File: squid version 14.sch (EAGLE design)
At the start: 61 parts, among them J2 ATMEL_PROGRAMMER_HEADERNL, U2 MCP73832

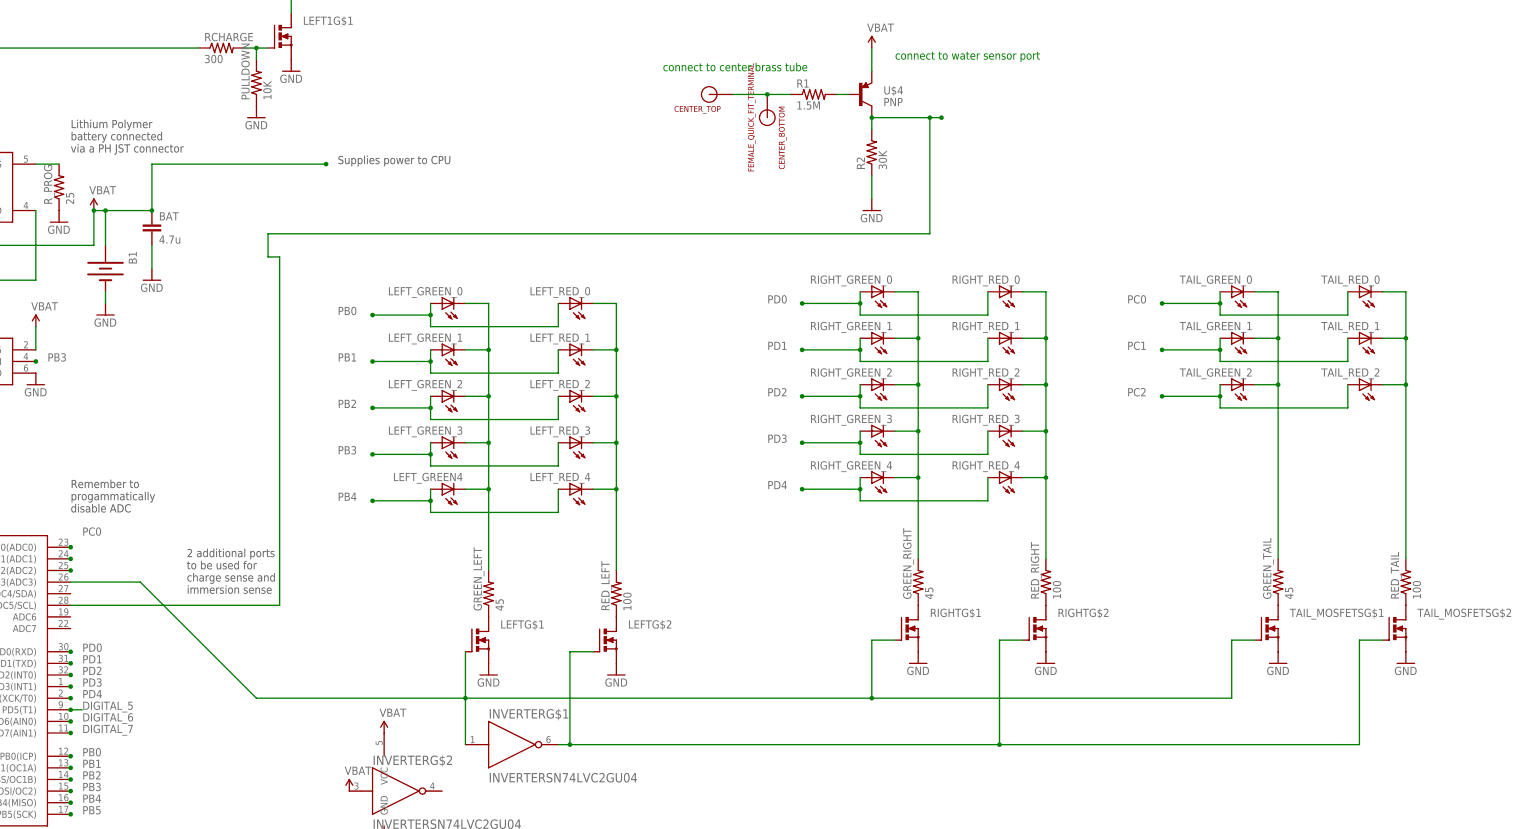
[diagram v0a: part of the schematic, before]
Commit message: put RG TH lights in rear
Rearranged board to hold TH parts in rear.
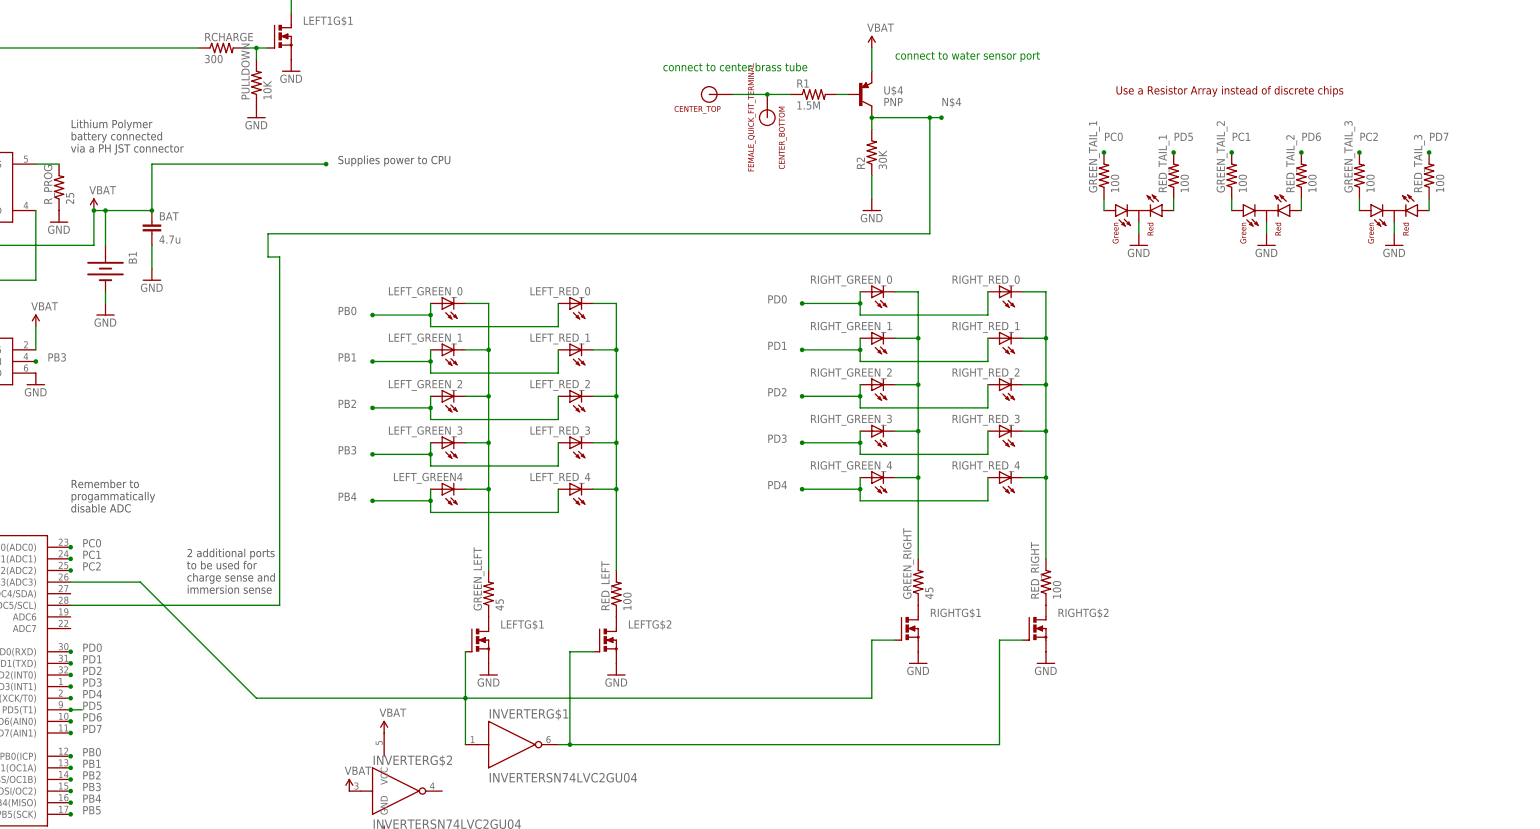
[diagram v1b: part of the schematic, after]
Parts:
- removed GREEN_TAIL: 45, SparkFun-Passives:RESISTOR0805-RES
- removed RED_TAIL: 100, SparkFun-Passives:RESISTOR0805-RES
- removed TAIL_GREEN_0, TAIL_GREEN_1, TAIL_GREEN_2, TAIL_RED_0, TAIL_RED_1, TAIL_RED_2: (no value), ERIC:LEDPLCC2
- removed TAIL_MOSFETS: MOSFET_N_DUAL, ERIC:MOSFET_N_DUAL
- added CENTER, U$13, U$7: LED_RED_GREEN_CC, ERIC:LED_RED_GREEN_CC
- added GREEN_TAIL_1, GREEN_TAIL_2, GREEN_TAIL_3, RED_TAIL_1, RED_TAIL_2, RED_TAIL_3: 100, SparkFun-Passives:RESISTOR0805-RES
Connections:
- removed net DIGITAL_5: U1.PD5(T1)
- removed net DIGITAL_6: U1.PD6(AIN0)
- removed net DIGITAL_7: U1.PD7(AIN1)
- removed net N$13: GREEN_TAIL.1, TAIL_MOSFETSG$1.D
- removed net N$18: RED_TAIL.1, TAIL_MOSFETSG$2.D
- removed net N$19: GREEN_TAIL.2, TAIL_GREEN_0.C, TAIL_GREEN_1.C, TAIL_GREEN_2.C
- new net N$17: GREEN_TAIL_1.1, U$7.GREEN
- new net N$22: GREEN_TAIL_3.1, U$13.GREEN
- new net N$23: RED_TAIL_1.1, U$7.RED
- new net N$24: CENTER.RED, RED_TAIL_2.1
- new net N$25: RED_TAIL_3.1, U$13.RED
- new net PD5: RED_TAIL_1.2, U1.PD5(T1)
- new net PD6: RED_TAIL_2.2, U1.PD6(AIN0)
- new net PD7: RED_TAIL_3.2, U1.PD7(AIN1)
- net GND: now also CENTER.C, U$13.C, U$7.C; no longer TAIL_MOSFETSG$1.S, TAIL_MOSFETSG$2.S
- net N$2: no longer TAIL_MOSFETSG$2.G
- net N$20: now also CENTER.GREEN, GREEN_TAIL_2.1; no longer RED_TAIL.2, TAIL_RED_0.C, TAIL_RED_1.C, TAIL_RED_2.C
- net N$7: no longer TAIL_MOSFETSG$1.G
- net PC0: now also GREEN_TAIL_1.2; no longer TAIL_GREEN_0.A, TAIL_RED_0.A
- net PC1: now also GREEN_TAIL_2.2; no longer TAIL_GREEN_1.A, TAIL_RED_1.A
- net PC2: now also GREEN_TAIL_3.2; no longer TAIL_GREEN_2.A, TAIL_RED_2.A
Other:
- note added: "Use a Resistor Array instead of discrete chips"

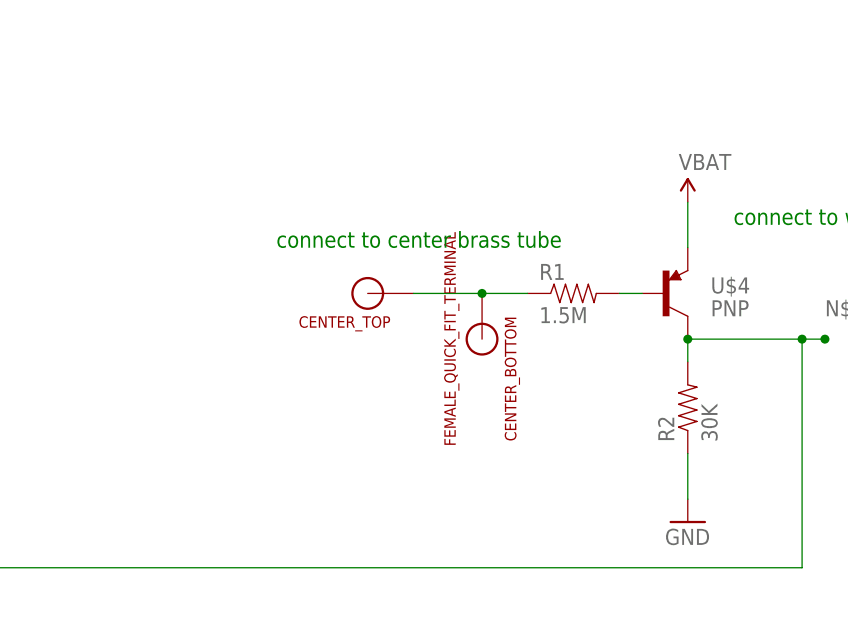
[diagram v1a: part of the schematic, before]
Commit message: disconnect top center tube holder
Does not need an electrical connection
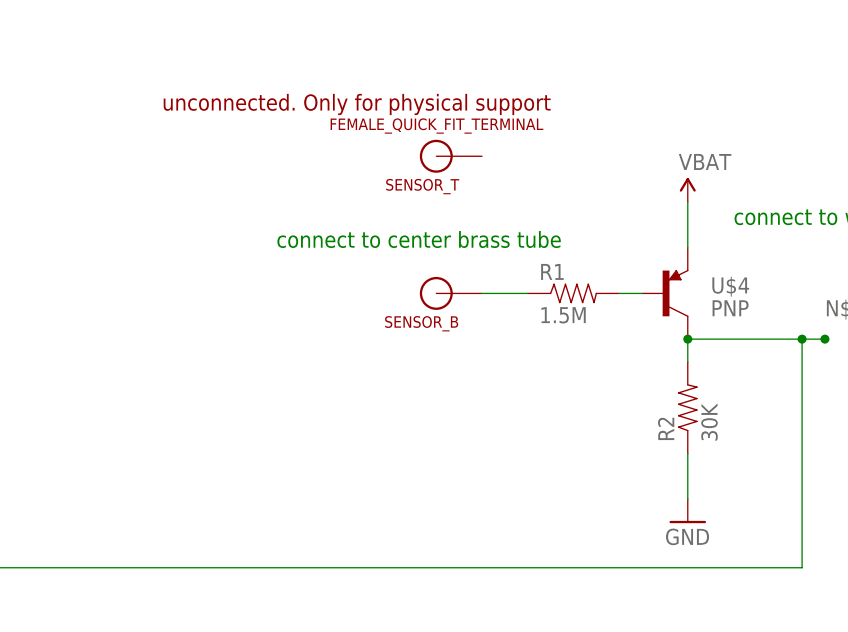
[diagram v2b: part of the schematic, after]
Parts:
- removed CENTER_BOTTOM, CENTER_TOP: FEMALE_QUICK_FIT_TERMINAL, Keystone:FEMALE_QUICK_FIT_TERMINAL
- added SENSOR_B, SENSOR_T: FEMALE_QUICK_FIT_TERMINAL, Keystone:FEMALE_QUICK_FIT_TERMINAL
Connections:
- net N$9: now also SENSOR_B.P$1; no longer CENTER_BOTTOM.P$1, CENTER_TOP.P$1
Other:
- note added: "unconnected. Only for physical support"
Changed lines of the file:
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@@
 <part name="RIGHT_RED_4" library="ERIC" deviceset="LED" device="PLCC2"/>
 <part name="RIGHT_RED_0" library="ERIC" deviceset="LED" device="PLCC2"/>
-<part name="CENTER_BOTTOM" library="Keystone" deviceset="FEMALE_QUICK_FIT_TERMINAL" device=""/>
-<part name="CENTER_TOP" library="Keystone" deviceset="FEMALE_QUICK_FIT_TERMINAL" device="" value=""/>
+<part name="SENSOR_T" library="Keystone" deviceset="FEMALE_QUICK_FIT_TERMINAL" device=""/>
+<part name="SENSOR_B" library="Keystone" deviceset="FEMALE_QUICK_FIT_TERMINAL" device="" value=""/>
 <part name="GND11" library="SparkFun" deviceset="GND" device=""/>
 <part name="U$14" library="ERIC" deviceset="VBAT" device=""/>
@@
 <text x="109.22" y="190.5" size="1.778" layer="91">RESET LOW when charging</text>
 <text x="330.2" y="167.64" size="1.778" layer="94">Use a Resistor Array instead of discrete chips</text>
+<text x="218.44" y="187.96" size="1.778" layer="94">unconnected. Only for physical support</text>
 </plain>
 <instances>
@@
 <instance part="RIGHT_RED_4" gate="G$1" x="307.34" y="83.82" rot="R90"/>
 <instance part="RIGHT_RED_0" gate="G$1" x="307.34" y="124.46" rot="R90"/>
-<instance part="CENTER_BOTTOM" gate="G$1" x="254" y="162.56" rot="R270"/>
-<instance part="CENTER_TOP" gate="G$1" x="241.3" y="167.64" rot="R180"/>
+<instance part="SENSOR_T" gate="G$1" x="248.92" y="182.88" rot="R180"/>
+<instance part="SENSOR_B" gate="G$1" x="248.92" y="167.64" rot="R180"/>
 <instance part="INVERTER" gate="G$2" x="172.72" y="15.24"/>
 <instance part="INVERTER" gate="G$3" x="170.18" y="20.32"/>
@@
 </segment>
 </net>
-<net name="N$9" class="0">
-<segment>
-<pinref part="R1" gate="G$1" pin="1"/>
-<pinref part="CENTER_BOTTOM" gate="G$1" pin="P$1"/>
-<wire x1="259.08" y1="167.64" x2="254" y2="167.64" width="0.1524" layer="91"/>
-<pinref part="CENTER_TOP" gate="G$1" pin="P$1"/>
-<wire x1="246.38" y1="167.64" x2="254" y2="167.64" width="0.1524" layer="91"/>
-<junction x="254" y="167.64"/>
-</segment>
-</net>
 <net name="N$21" class="0">
 <segment>
@@
 </segment>
 </net>
+<net name="N$9" class="0">
+<segment>
+<pinref part="R1" gate="G$1" pin="1"/>
+<pinref part="SENSOR_B" gate="G$1" pin="P$1"/>
+<wire x1="254" y1="167.64" x2="259.08" y2="167.64" width="0.1524" layer="91"/>
+</segment>
+</net>

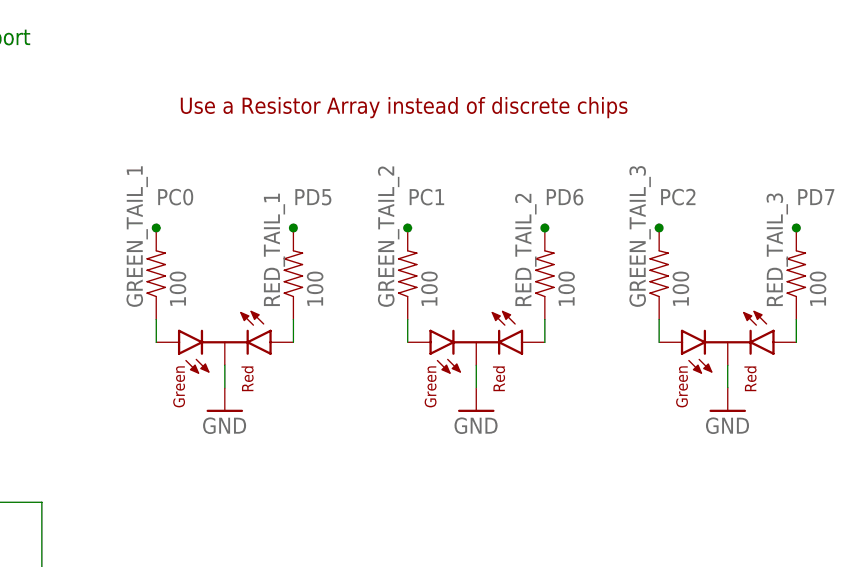
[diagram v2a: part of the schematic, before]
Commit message: assign values of ballast resistors
Put proper values of ballast resistors into schematic
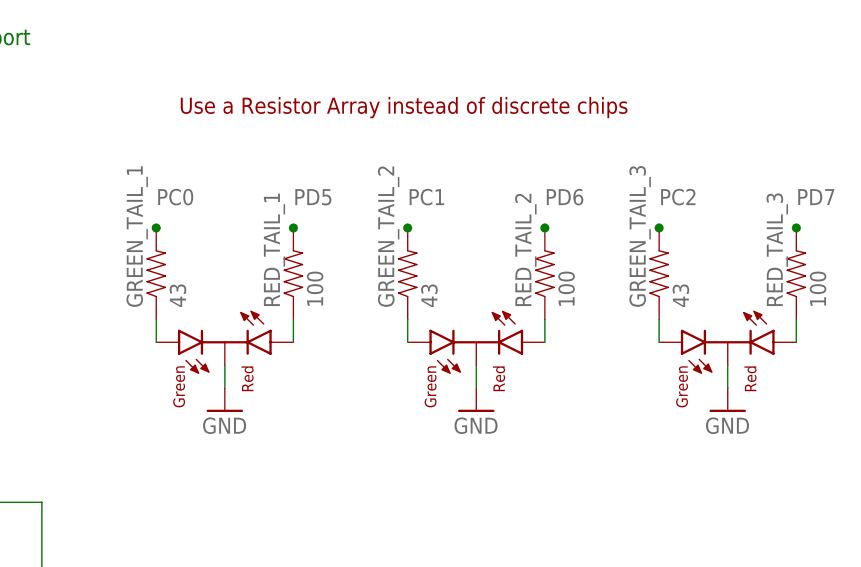
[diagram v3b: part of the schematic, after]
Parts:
- GREEN_TAIL_1, GREEN_TAIL_2, GREEN_TAIL_3: value 100 -> 43
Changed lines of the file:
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@@
 <part name="GND18" library="SparkFun" deviceset="GND" device=""/>
 <part name="GND22" library="SparkFun" deviceset="GND" device=""/>
-<part name="GREEN_TAIL_1" library="SparkFun-Passives" deviceset="RESISTOR" device="0805-RES" value="100"/>
-<part name="GREEN_TAIL_2" library="SparkFun-Passives" deviceset="RESISTOR" device="0805-RES" value="100"/>
-<part name="GREEN_TAIL_3" library="SparkFun-Passives" deviceset="RESISTOR" device="0805-RES" value="100"/>
+<part name="GREEN_TAIL_1" library="SparkFun-Passives" deviceset="RESISTOR" device="0805-RES" value="43"/>
+<part name="GREEN_TAIL_2" library="SparkFun-Passives" deviceset="RESISTOR" device="0805-RES" value="43"/>
+<part name="GREEN_TAIL_3" library="SparkFun-Passives" deviceset="RESISTOR" device="0805-RES" value="43"/>
 <part name="RED_TAIL_1" library="SparkFun-Passives" deviceset="RESISTOR" device="0805-RES" value="100"/>
 <part name="RED_TAIL_2" library="SparkFun-Passives" deviceset="RESISTOR" device="0805-RES" value="100"/>

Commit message: correct current programming resistor value
Major mistake in current programming resistor!! Changed from 24 to
4.7K!!!
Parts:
- GREEN_TAIL_1, GREEN_TAIL_2, GREEN_TAIL_3: value 43 -> 45
- R_PROG: value 25 -> 4.7K
- renumbered LEFT1 to CHARGING, U$10 to GND_BOT, U$17 to GND_TOP, U$8 to CHARGE_TOP
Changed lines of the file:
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@@
 <part name="GND19" library="SparkFun" deviceset="GND" device=""/>
 <part name="GND20" library="SparkFun" deviceset="GND" device=""/>
-<part name="R_PROG" library="SparkFun" deviceset="RESISTOR" device="0805-RES" value="25"/>
+<part name="R_PROG" library="SparkFun" deviceset="RESISTOR" device="0805-RES" value="4.7K"/>
 <part name="GND21" library="SparkFun" deviceset="GND" device=""/>
 <part name="LED" library="led" deviceset="LED" device="CHIP-LED0805" value="RED"/>
@@
 <part name="B1" library="Keystone" deviceset="COIN_CELL_BATTERY" device="JST"/>
 <part name="U$6" library="ERIC" deviceset="VBAT" device=""/>
-<part name="U$8" library="Keystone" deviceset="FEMALE_QUICK_FIT_TERMINAL" device=""/>
-<part name="U$10" library="Keystone" deviceset="FEMALE_QUICK_FIT_TERMINAL" device=""/>
+<part name="CHARGE_TOP" library="Keystone" deviceset="FEMALE_QUICK_FIT_TERMINAL" device=""/>
+<part name="GND_BOT" library="Keystone" deviceset="FEMALE_QUICK_FIT_TERMINAL" device=""/>
 <part name="GND14" library="SparkFun-Aesthetics" deviceset="GND" device=""/>
 <part name="U$11" library="ERIC" deviceset="VCHARGE" device=""/>
@@
 <part name="GND10" library="SparkFun" deviceset="GND" device=""/>
 <part name="CHARGE_BOTTOM" library="Keystone" deviceset="FEMALE_QUICK_FIT_TERMINAL" device=""/>
-<part name="U$17" library="Keystone" deviceset="FEMALE_QUICK_FIT_TERMINAL" device=""/>
+<part name="GND_TOP" library="Keystone" deviceset="FEMALE_QUICK_FIT_TERMINAL" device=""/>
 <part name="GND12" library="SparkFun-Aesthetics" deviceset="GND" device=""/>
-<part name="LEFT1" library="ERIC" deviceset="MOSFET_N_DUAL" device=""/>
+<part name="CHARGING" library="ERIC" deviceset="MOSFET_N_DUAL" device=""/>
 <part name="GND13" library="SparkFun" deviceset="GND" device=""/>
 <part name="RCHARGE" library="SparkFun" deviceset="RESISTOR" device="0805-RES" value="300"/>
@@
 <part name="GND18" library="SparkFun" deviceset="GND" device=""/>
 <part name="GND22" library="SparkFun" deviceset="GND" device=""/>
-<part name="GREEN_TAIL_1" library="SparkFun-Passives" deviceset="RESISTOR" device="0805-RES" value="43"/>
-<part name="GREEN_TAIL_2" library="SparkFun-Passives" deviceset="RESISTOR" device="0805-RES" value="43"/>
-<part name="GREEN_TAIL_3" library="SparkFun-Passives" deviceset="RESISTOR" device="0805-RES" value="43"/>
+<part name="GREEN_TAIL_1" library="SparkFun-Passives" deviceset="RESISTOR" device="0805-RES" value="45"/>
+<part name="GREEN_TAIL_2" library="SparkFun-Passives" deviceset="RESISTOR" device="0805-RES" value="45"/>
+<part name="GREEN_TAIL_3" library="SparkFun-Passives" deviceset="RESISTOR" device="0805-RES" value="45"/>
 <part name="RED_TAIL_1" library="SparkFun-Passives" deviceset="RESISTOR" device="0805-RES" value="100"/>
 <part name="RED_TAIL_2" library="SparkFun-Passives" deviceset="RESISTOR" device="0805-RES" value="100"/>
@@
 </instance>
 <instance part="U$6" gate="G$1" x="106.68" y="142.24"/>
-<instance part="U$8" gate="G$1" x="15.24" y="96.52" rot="R270"/>
-<instance part="U$10" gate="G$1" x="30.48" y="96.52" rot="R270"/>
+<instance part="CHARGE_TOP" gate="G$1" x="15.24" y="96.52" rot="R270"/>
+<instance part="GND_BOT" gate="G$1" x="30.48" y="96.52" rot="R270"/>
 <instance part="GND14" gate="1" x="30.48" y="104.14" rot="R180"/>
 <instance part="U$11" gate="G$1" x="15.24" y="101.6"/>
@@
 <instance part="GND10" gate="1" x="276.86" y="142.24"/>
 <instance part="CHARGE_BOTTOM" gate="G$1" x="2.54" y="96.52" rot="R270"/>
-<instance part="U$17" gate="G$1" x="40.64" y="96.52" rot="R270"/>
+<instance part="GND_TOP" gate="G$1" x="40.64" y="96.52" rot="R270"/>
 <instance part="GND12" gate="1" x="40.64" y="104.14" rot="R180"/>
-<instance part="LEFT1" gate="G$1" x="147.32" y="180.34"/>
+<instance part="CHARGING" gate="G$1" x="147.32" y="180.34"/>
 <instance part="GND13" gate="1" x="149.86" y="172.72"/>
 <instance part="RCHARGE" gate="G$1" x="134.62" y="177.8"/>
@@
 </segment>
 <segment>
-<pinref part="U$10" gate="G$1" pin="P$1"/>
+<pinref part="GND_BOT" gate="G$1" pin="P$1"/>
 <pinref part="GND14" gate="1" pin="GND"/>
 </segment>
@@
 </segment>
 <segment>
-<pinref part="U$17" gate="G$1" pin="P$1"/>
+<pinref part="GND_TOP" gate="G$1" pin="P$1"/>
 <pinref part="GND12" gate="1" pin="GND"/>
 </segment>
 <segment>
-<pinref part="LEFT1" gate="G$1" pin="S"/>
+<pinref part="CHARGING" gate="G$1" pin="S"/>
 <pinref part="GND13" gate="1" pin="GND"/>
 </segment>
@@
 <net name="RESET" class="0">
 <segment>
-<pinref part="LEFT1" gate="G$1" pin="D"/>
+<pinref part="CHARGING" gate="G$1" pin="D"/>
 <wire x1="149.86" y1="185.42" x2="149.86" y2="195.58" width="0.1524" layer="91"/>
 <junction x="149.86" y="195.58"/>
@@
 <net name="VCHARGE" class="0">
 <segment>
-<pinref part="U$8" gate="G$1" pin="P$1"/>
+<pinref part="CHARGE_TOP" gate="G$1" pin="P$1"/>
 <pinref part="U$11" gate="G$1" pin="VCHARGE"/>
 </segment>
@@
 <net name="N$3" class="0">
 <segment>
-<pinref part="LEFT1" gate="G$1" pin="G"/>
+<pinref part="CHARGING" gate="G$1" pin="G"/>
 <pinref part="RCHARGE" gate="G$1" pin="2"/>
 <wire x1="139.7" y1="177.8" x2="142.24" y2="177.8" width="0.1524" layer="91"/>
